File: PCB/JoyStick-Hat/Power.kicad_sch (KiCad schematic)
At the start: 17 parts, among them J6 1757242, J9 1755736, M1 D24V22F12, M2 D24V22F5, M3 D24V22F3

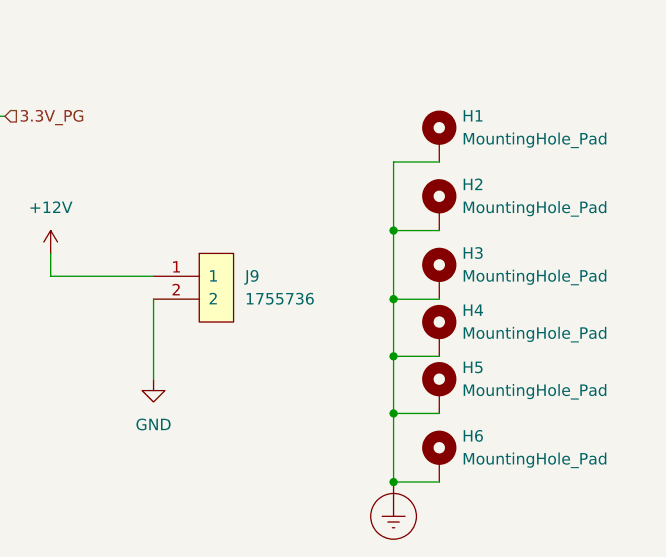
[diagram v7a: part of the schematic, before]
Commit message: Connectors Moved, Labels Added, and New Images
Moved connectors around so labels can be fit on the bottom of PCB, labels added to bottom of PCB. New images exported !
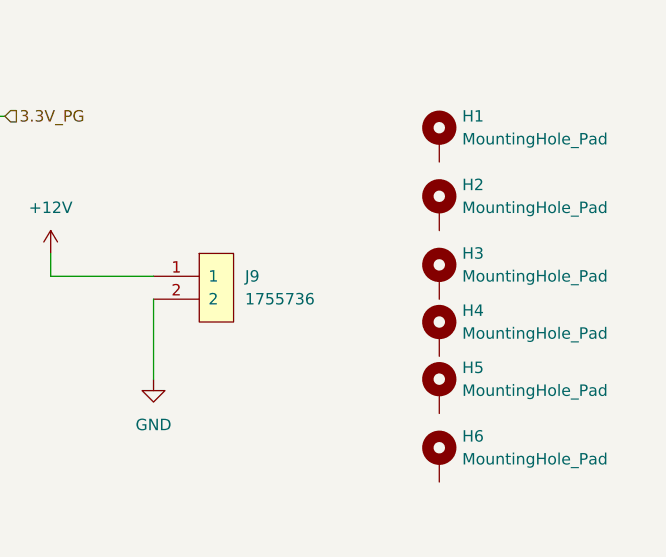
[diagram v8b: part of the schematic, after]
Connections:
- removed net Earth_Protective: H1.1, H2.1, H3.1, H4.1, H5.1, H6.1
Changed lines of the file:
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@@
-	)
-	(junction
-		(at 209.55 135.89)
-		(diameter 0)
-		(color 0 0 0 0)
 	)
 	(junction
@@
 	)
 	(junction
-		(at 209.55 149.86)
-		(diameter 0)
-		(color 0 0 0 0)
-	)
-	(junction
-		(at 209.55 121.92)
-		(diameter 0)
-		(color 0 0 0 0)
-	)
-	(junction
 		(at 124.46 127)
 		(diameter 0)
@@
 	)
 	(junction
-		(at 209.55 142.24)
-		(diameter 0)
-		(color 0 0 0 0)
-	)
-	(junction
 		(at 99.06 127)
 		(diameter 0)
 		(color 0 0 0 0)
 	)
-	(junction
-		(at 209.55 129.54)
-		(diameter 0)
-		(color 0 0 0 0)
-	)
 	(wire
 		(pts
@@
 	(wire
 		(pts
-			(xy 209.55 135.89) (xy 214.63 135.89)
-		)
-		(stroke
-			(width 0)
-			(type default)
-		)
-	)
-	(wire
-		(pts
 			(xy 111.76 138.43) (xy 124.46 138.43)
 		)
@@
 	(wire
 		(pts
-			(xy 214.63 114.3) (xy 209.55 114.3)
-		)
-		(stroke
-			(width 0)
-			(type default)
-		)
-	)
-	(wire
-		(pts
 			(xy 137.16 83.82) (xy 166.37 83.82)
 		)
@@
 	(wire
 		(pts
-			(xy 209.55 149.86) (xy 214.63 149.86)
-		)
-		(stroke
-			(width 0)
-			(type default)
-		)
-	)
-	(wire
-		(pts
 			(xy 124.46 127) (xy 135.89 127)
 		)
@@
 	(wire
 		(pts
-			(xy 209.55 142.24) (xy 209.55 149.86)
-		)
-		(stroke
-			(width 0)
-			(type default)
-		)
-	)
-	(wire
-		(pts
 			(xy 135.89 138.43) (xy 135.89 129.54)
 		)
@@
 	(wire
 		(pts
-			(xy 209.55 129.54) (xy 209.55 135.89)
-		)
-		(stroke
-			(width 0)
-			(type default)
-		)
-	)
-	(wire
-		(pts
 			(xy 171.45 127) (xy 182.88 127)
 		)
@@
 	(wire
 		(pts
-			(xy 209.55 129.54) (xy 214.63 129.54)
-		)
-		(stroke
-			(width 0)
-			(type default)
-		)
-	)
-	(wire
-		(pts
 			(xy 182.88 129.54) (xy 182.88 138.43)
 		)
@@
 	(wire
 		(pts
-			(xy 209.55 142.24) (xy 214.63 142.24)
-		)
-		(stroke
-			(width 0)
-			(type default)
-		)
-	)
-	(wire
-		(pts
 			(xy 111.76 127) (xy 124.46 127)
 		)
@@
 	(wire
 		(pts
-			(xy 209.55 121.92) (xy 209.55 129.54)
-		)
-		(stroke
-			(width 0)
-			(type default)
-		)
-	)
-	(wire
-		(pts
 			(xy 138.43 58.42) (xy 166.37 58.42)
 		)
@@
 	(wire
 		(pts
-			(xy 209.55 114.3) (xy 209.55 121.92)
-		)
-		(stroke
-			(width 0)
-			(type default)
-		)
-	)
-	(wire
-		(pts
-			(xy 209.55 121.92) (xy 214.63 121.92)
-		)
-		(stroke
-			(width 0)
-			(type default)
-		)
-	)
-	(wire
-		(pts
 			(xy 90.17 77.47) (xy 99.06 77.47)
 		)
@@
 		(pts
 			(xy 137.16 109.22) (xy 166.37 109.22)
-		)
-		(stroke
-			(width 0)
-			(type default)
-		)
-	)
-	(wire
-		(pts
-			(xy 209.55 135.89) (xy 209.55 142.24)
 		)
 		(stroke
@@
 					(unit 1)
 				)
-			)
-		)
-	)
-	(symbol
-		(lib_id "power:Earth_Protective")
-		(at 209.55 149.86 0)
-		(unit 1)
-		(exclude_from_sim no)
-		(in_bom yes)
-		(on_board yes)
-		(dnp no)
-		(fields_autoplaced yes)
-		(property "Reference" "#PWR025"
-			(at 215.9 156.21 0)
-			(effects
-				(font
-					(size 1.27 1.27)
-				)
-				(hide yes)
-			)
-		)
-		(property "Value" "Earth_Protective"
-			(at 220.98 153.67 0)
-			(effects
-				(font
-					(size 1.27 1.27)
-				)
-				(hide yes)
-			)
-		)
-		(property "Footprint" ""
-			(at 209.55 152.4 0)
-			(effects
-				(font
-					(size 1.27 1.27)
-				)
-				(hide yes)
-			)
-		)
-		(property "Datasheet" "~"
-			(at 209.55 152.4 0)
-			(effects
-				(font
-					(size 1.27 1.27)
-				)
-				(hide yes)
-			)
-		)
-		(property "Description" ""
-			(at 209.55 149.86 0)
-			(effects
-				(font
-					(size 1.27 1.27)
-				)
-				(hide yes)
-			)
-		)
-		(pin "1"
-		)
-		(instances
-			(project "JoyStick-Hat"
-				(path "/cf0c81b5-5bdf-47c3-83c0-f6980f515e65/e93621b0-f51d-4ad7-baf5-6493a8f9cdb5"
-					(reference "#PWR025")
-					(unit 1)
-				)
